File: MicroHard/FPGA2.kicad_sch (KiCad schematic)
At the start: 1 part, among them U4 XC7A100T-FTG256

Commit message: feat: finished config
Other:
- moved on the sheet: U4B
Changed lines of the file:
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@@
 	(symbol
 		(lib_id "FPGA_Xilinx_Artix7:XC7A100T-FTG256")
-		(at 87.63 99.06 0)
+		(at 142.24 91.44 0)
 		(unit 2)
 		(exclude_from_sim no)
@@
 		(fields_autoplaced yes)
 		(property "Reference" "U4"
-			(at 87.63 175.26 0)
+			(at 142.24 167.64 0)
 			(effects
 				(font
@@
 		)
 		(property "Value" "XC7A100T-FTG256"
-			(at 87.63 177.8 0)
+			(at 142.24 170.18 0)
 			(effects
 				(font
@@
 		)
 		(property "Footprint" ""
-			(at 87.63 99.06 0)
+			(at 142.24 91.44 0)
 			(effects
 				(font
@@
 		)
 		(property "Datasheet" ""
-			(at 87.63 99.06 0)
+			(at 142.24 91.44 0)
 			(effects
 				(font
@@
 		)
 		(property "Description" "Artix 7 T 100 XC7A100T-FTG256"
-			(at 87.63 99.06 0)
+			(at 142.24 91.44 0)
 			(effects
 				(font

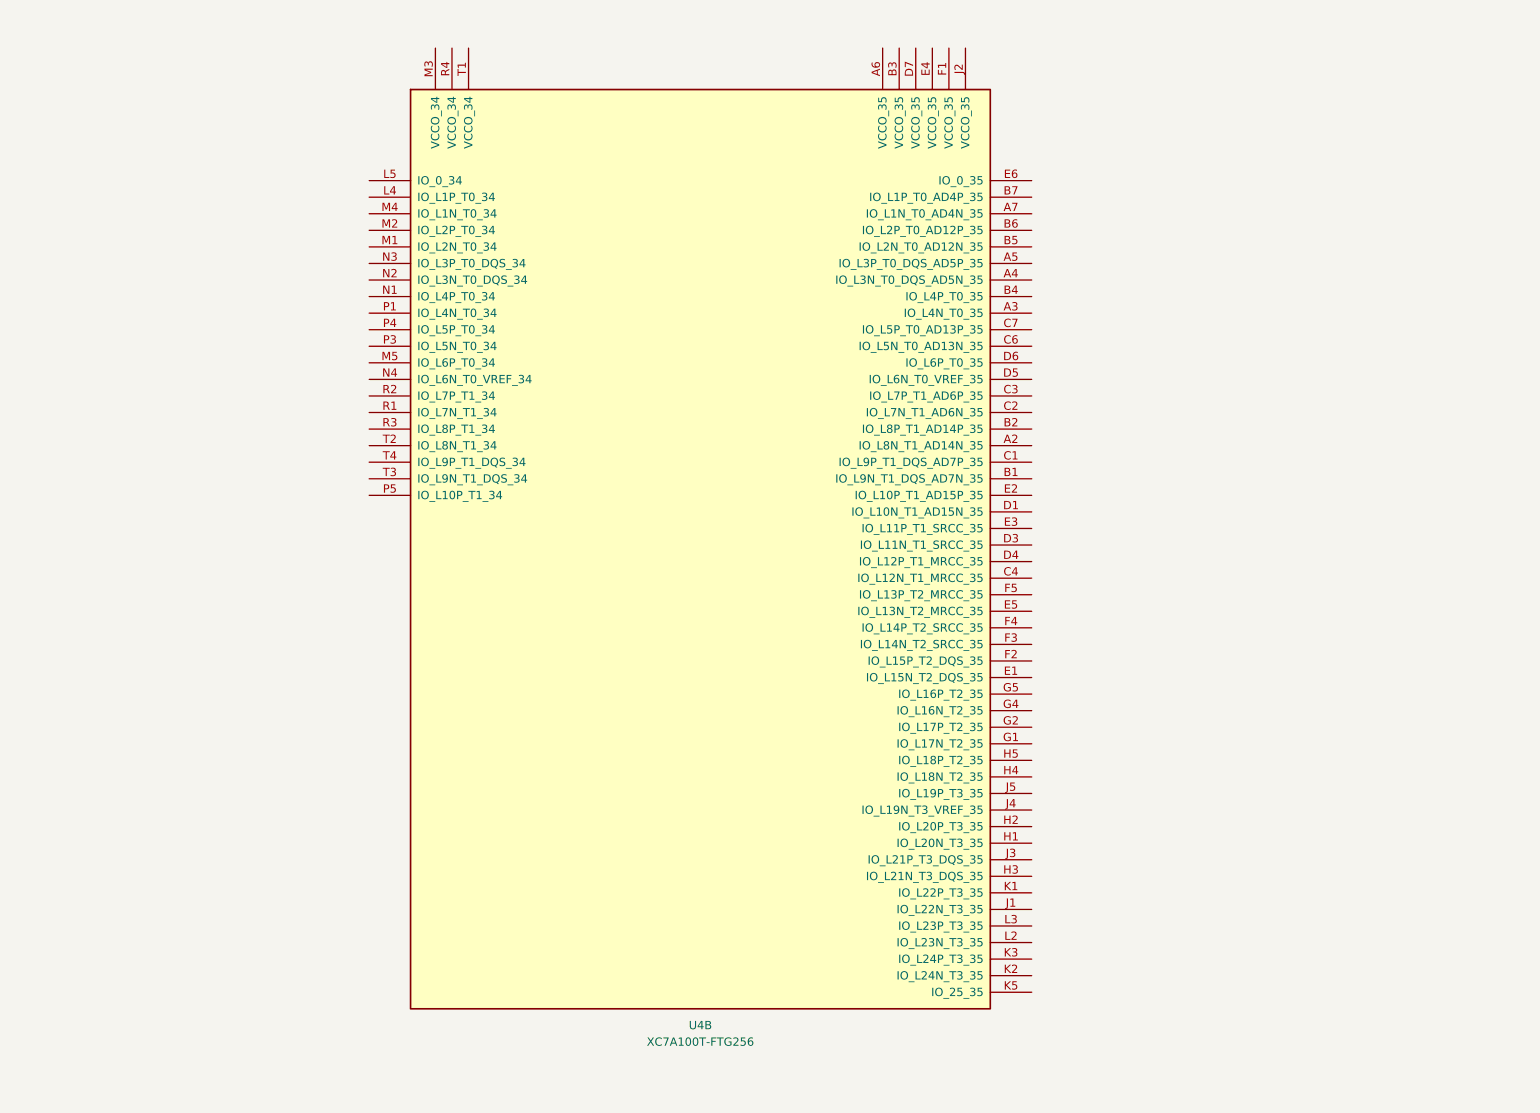
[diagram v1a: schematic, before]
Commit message: feat: added VGA signal out from FPGA
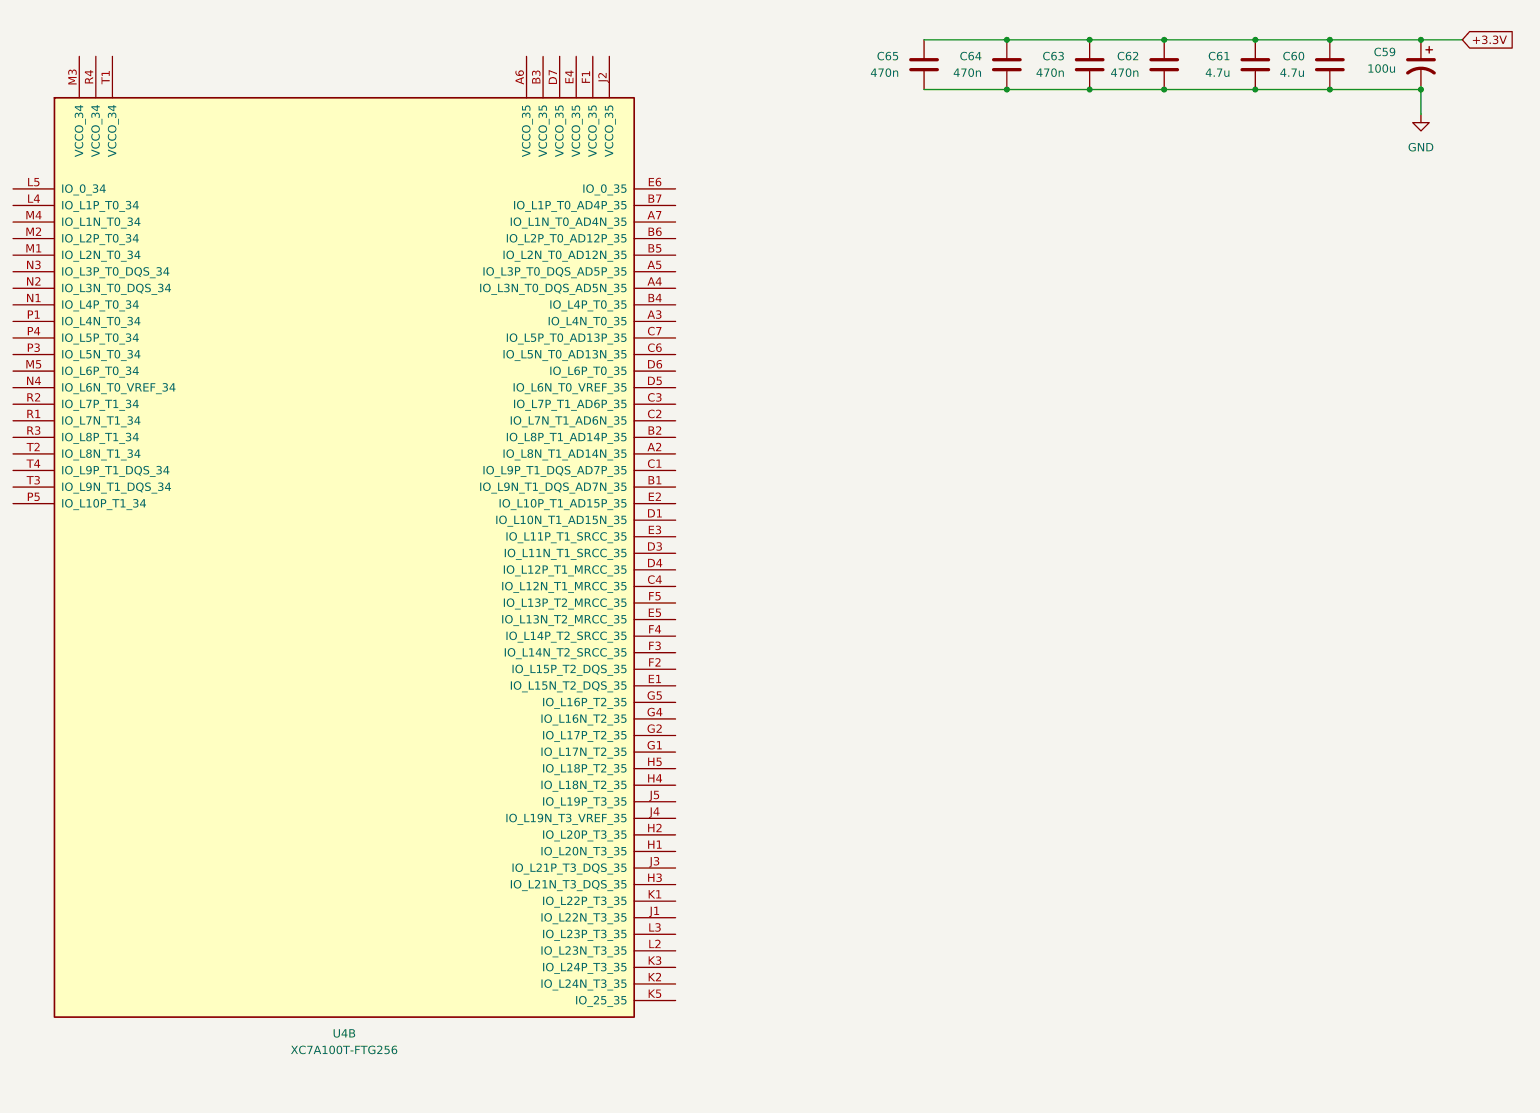
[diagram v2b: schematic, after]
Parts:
- added C59: 100u, symbol Device:C_Polarized_US
- added C60, C61: 4.7u, symbol Device:C
- added C62, C63, C64, C65: 470n, symbol Device:C
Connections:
- new net +3.3V: C59.1, C60.1, C61.1, C62.1, C63.1, C64.1, C65.1
- new net GND: C59.2, C60.2, C61.2, C62.2, C63.2, C64.2, C65.2
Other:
- moved on the sheet: U4B

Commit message: feat: VGA out lines from FPGA drawn
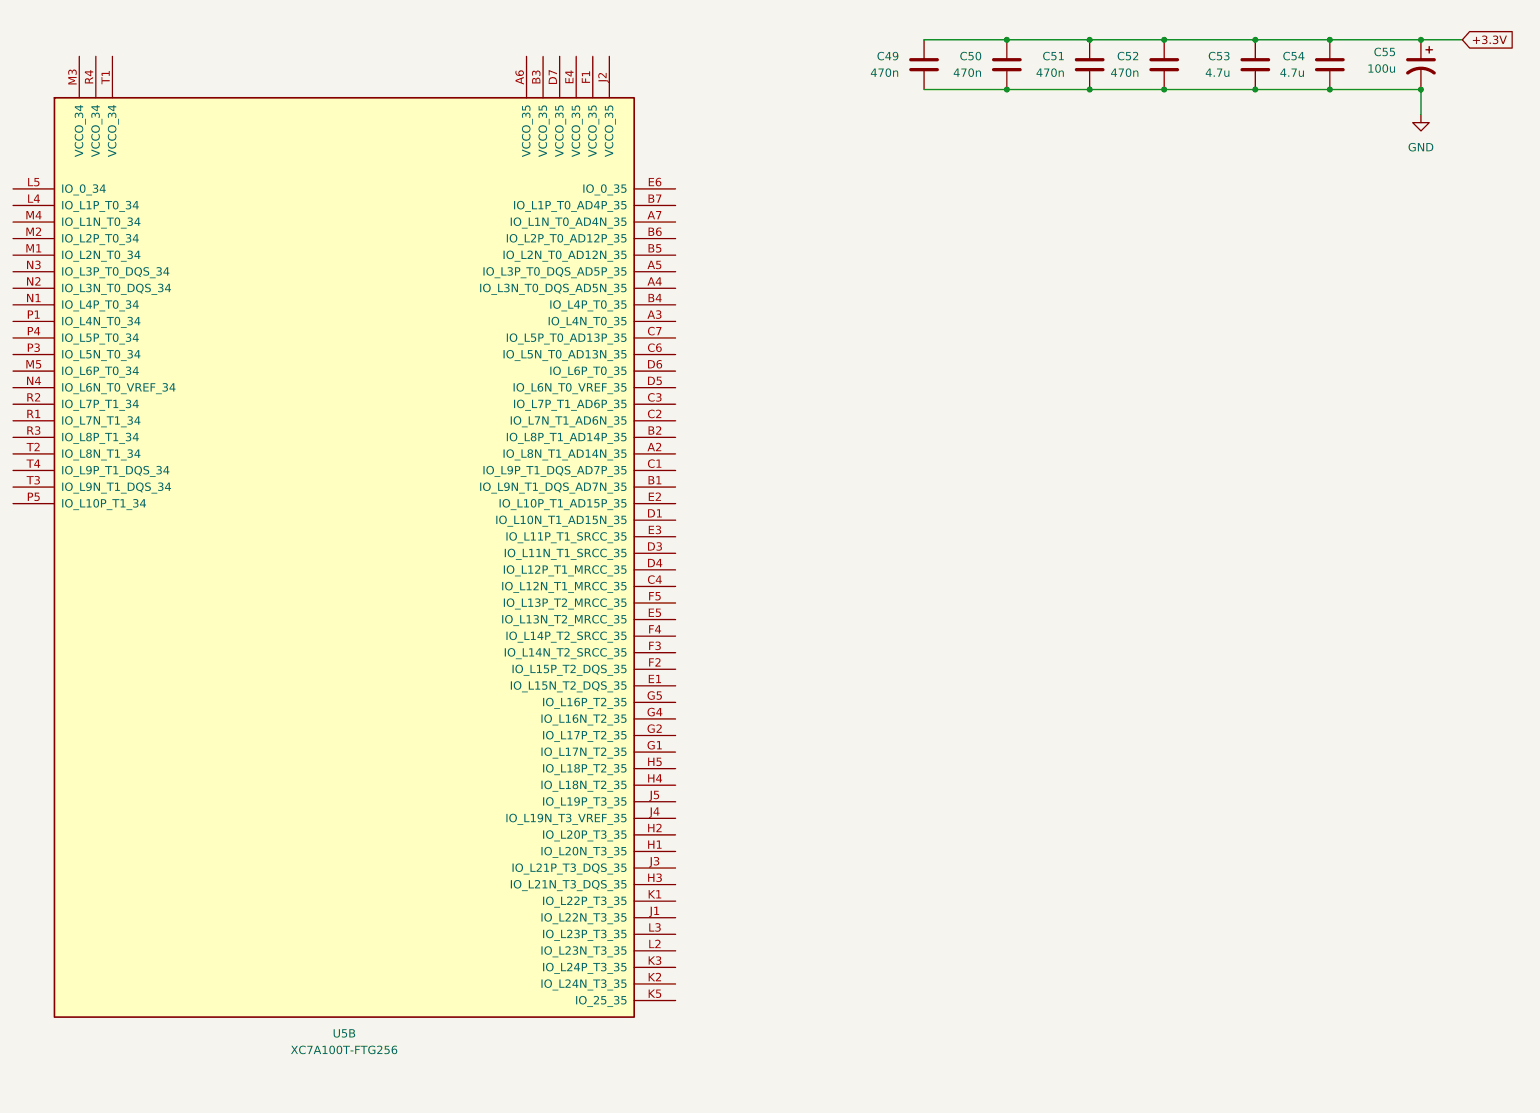
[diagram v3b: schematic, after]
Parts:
- renumbered C65 to C49, C64 to C50, C63 to C51, C62 to C52, C61 to C53, C60 to C54, C59 to C55, U4 to U5
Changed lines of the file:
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@@
 		(dnp no)
 		(fields_autoplaced yes)
-		(property "Reference" "#PWR035"
+		(property "Reference" "#PWR029"
 			(at 252.73 34.29 0)
 			(effects
@@
 			(project "MicroHard"
 				(path "/578bd531-a491-4b15-a479-460d159ffc14/e381883e-e672-4900-88a5-08b94f970a88/3b40193c-1579-4de8-9c25-9c04775413b4"
-					(reference "#PWR035")
+					(reference "#PWR029")
 					(unit 1)
 				)
@@
 		(dnp no)
 		(fields_autoplaced yes)
-		(property "Reference" "C64"
+		(property "Reference" "C50"
 			(at 185.42 19.0499 0)
 			(effects
@@
 			(project "MicroHard"
 				(path "/578bd531-a491-4b15-a479-460d159ffc14/e381883e-e672-4900-88a5-08b94f970a88/3b40193c-1579-4de8-9c25-9c04775413b4"
-					(reference "C64")
+					(reference "C50")
 					(unit 1)
 				)
@@
 		(dnp no)
 		(fields_autoplaced yes)
-		(property "Reference" "U4"
+		(property "Reference" "U5"
 			(at 87.63 168.91 0)
 			(effects
@@
 			(project "MicroHard"
 				(path "/578bd531-a491-4b15-a479-460d159ffc14/e381883e-e672-4900-88a5-08b94f970a88/3b40193c-1579-4de8-9c25-9c04775413b4"
-					(reference "U4")
+					(reference "U5")
 					(unit 2)
 				)
@@
 		(dnp no)
 		(fields_autoplaced yes)
-		(property "Reference" "C60"
+		(property "Reference" "C54"
 			(at 234.95 19.0499 0)
 			(effects
@@
 			(project "MicroHard"
 				(path "/578bd531-a491-4b15-a479-460d159ffc14/e381883e-e672-4900-88a5-08b94f970a88/3b40193c-1579-4de8-9c25-9c04775413b4"
-					(reference "C60")
+					(reference "C54")
 					(unit 1)
 				)
@@
 		(dnp no)
 		(fields_autoplaced yes)
-		(property "Reference" "C59"
+		(property "Reference" "C55"
 			(at 248.92 18.4149 0)
 			(effects
@@
 			(project "MicroHard"
 				(path "/578bd531-a491-4b15-a479-460d159ffc14/e381883e-e672-4900-88a5-08b94f970a88/3b40193c-1579-4de8-9c25-9c04775413b4"
-					(reference "C59")
+					(reference "C55")
 					(unit 1)
 				)
@@
 		(dnp no)
 		(fields_autoplaced yes)
-		(property "Reference" "C62"
+		(property "Reference" "C52"
 			(at 209.55 19.0499 0)
 			(effects
@@
 			(project "MicroHard"
 				(path "/578bd531-a491-4b15-a479-460d159ffc14/e381883e-e672-4900-88a5-08b94f970a88/3b40193c-1579-4de8-9c25-9c04775413b4"
-					(reference "C62")
+					(reference "C52")
 					(unit 1)
 				)
@@
 		(dnp no)
 		(fields_autoplaced yes)
-		(property "Reference" "C65"
+		(property "Reference" "C49"
 			(at 172.72 19.0499 0)
 			(effects
@@
 			(project "MicroHard"
 				(path "/578bd531-a491-4b15-a479-460d159ffc14/e381883e-e672-4900-88a5-08b94f970a88/3b40193c-1579-4de8-9c25-9c04775413b4"
-					(reference "C65")
+					(reference "C49")
 					(unit 1)
 				)
@@
 		(dnp no)
 		(fields_autoplaced yes)
-		(property "Reference" "C61"
+		(property "Reference" "C53"
 			(at 223.52 19.0499 0)
 			(effects
@@
 			(project "MicroHard"
 				(path "/578bd531-a491-4b15-a479-460d159ffc14/e381883e-e672-4900-88a5-08b94f970a88/3b40193c-1579-4de8-9c25-9c04775413b4"
-					(reference "C61")
+					(reference "C53")
 					(unit 1)
 				)
@@
 		(dnp no)
 		(fields_autoplaced yes)
-		(property "Reference" "C63"
+		(property "Reference" "C51"
 			(at 198.12 19.0499 0)
 			(effects
@@
 			(project "MicroHard"
 				(path "/578bd531-a491-4b15-a479-460d159ffc14/e381883e-e672-4900-88a5-08b94f970a88/3b40193c-1579-4de8-9c25-9c04775413b4"
-					(reference "C63")
+					(reference "C51")
 					(unit 1)
 				)

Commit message: feat: finished schematic, TODO: go through checklist
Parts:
- removed C49, C50, C51, C52: 470n, symbol Device:C
- removed C53, C54: 4.7u, symbol Device:C
- removed C55: 100u, symbol Device:C_Polarized_US
- U5: footprint (none) -> MicroHard:BGA256C100P16X16_1700X1700X155
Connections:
- no-connect marks 0 -> 79
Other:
- moved on the sheet: U5B

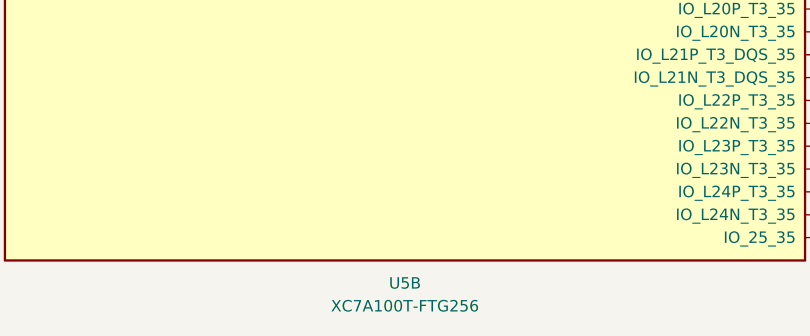
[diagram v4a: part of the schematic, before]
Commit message: Renumber parts
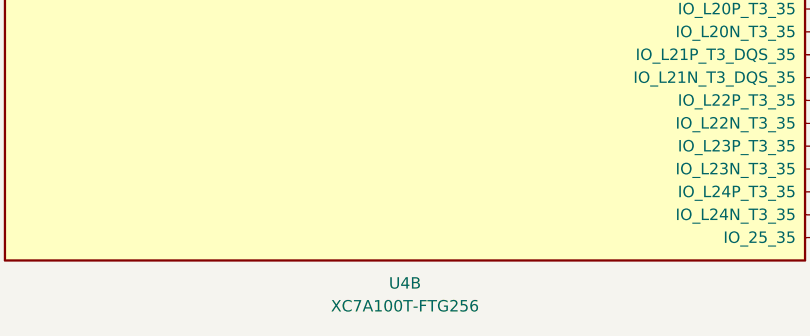
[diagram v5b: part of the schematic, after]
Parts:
- renumbered U5 to U4
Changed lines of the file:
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@@
 		(dnp no)
 		(fields_autoplaced yes)
-		(property "Reference" "U5"
+		(property "Reference" "U4"
 			(at 125.73 167.64 0)
 			(effects
@@
 			(project "MicroHard"
 				(path "/578bd531-a491-4b15-a479-460d159ffc14/e381883e-e672-4900-88a5-08b94f970a88/3b40193c-1579-4de8-9c25-9c04775413b4"
-					(reference "U5")
+					(reference "U4")
 					(unit 2)
 				)

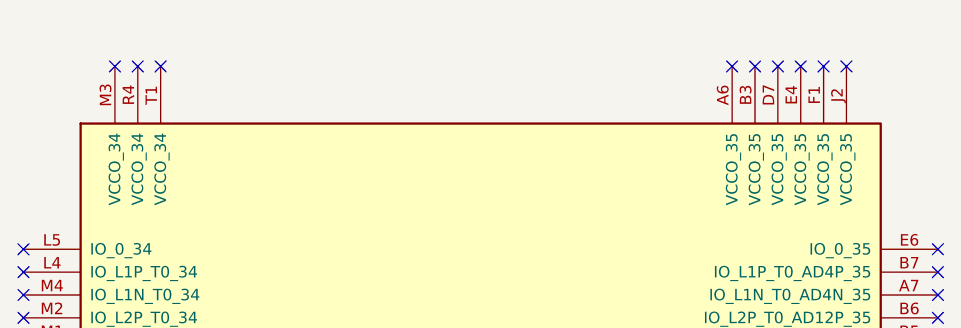
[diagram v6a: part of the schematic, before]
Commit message: power plane
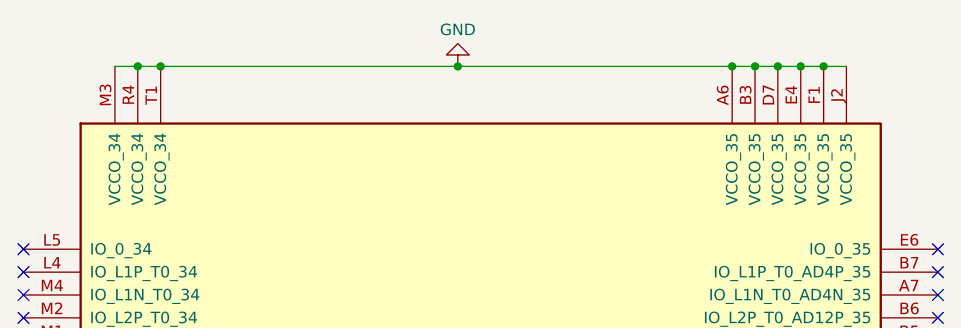
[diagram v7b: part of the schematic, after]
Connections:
- net GND: now reaches U4.A6 (VCCO_35)
- net GND: now also U4.B3 (VCCO_35), U4.D7 (VCCO_35), U4.E4 (VCCO_35), U4.F1 (VCCO_35), U4.J2 (VCCO_35), U4.M3 (VCCO_34), U4.R4 (VCCO_34), U4.T1 (VCCO_34)
- no-connect marks 79 -> 70
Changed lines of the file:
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@@
 	(generator_version "8.0")
 	(paper "A4")
+	(junction
+		(at 153.67 17.78)
+		(diameter 0)
+		(color 0 0 0 0)
+	)
+	(junction
+		(at 161.29 17.78)
+		(diameter 0)
+		(color 0 0 0 0)
+	)
+	(junction
+		(at 163.83 17.78)
+		(diameter 0)
+		(color 0 0 0 0)
+	)
+	(junction
+		(at 90.17 17.78)
+		(diameter 0)
+		(color 0 0 0 0)
+	)
+	(junction
+		(at 123.19 17.78)
+		(diameter 0)
+		(color 0 0 0 0)
+	)
+	(junction
+		(at 87.63 17.78)
+		(diameter 0)
+		(color 0 0 0 0)
+	)
+	(junction
+		(at 158.75 17.78)
+		(diameter 0)
+		(color 0 0 0 0)
+	)
+	(junction
+		(at 156.21 17.78)
+		(diameter 0)
+		(color 0 0 0 0)
+	)
 	(no_connect
 		(at 176.53 68.58)
@@
 	)
 	(no_connect
-		(at 90.17 17.78)
-	)
-	(no_connect
 		(at 176.53 147.32)
 	)
@@
 	)
 	(no_connect
-		(at 156.21 17.78)
-	)
-	(no_connect
-		(at 85.09 17.78)
-	)
-	(no_connect
 		(at 74.93 58.42)
 	)
@@
 	)
 	(no_connect
-		(at 153.67 17.78)
-	)
-	(no_connect
 		(at 74.93 48.26)
 	)
@@
 	)
 	(no_connect
-		(at 163.83 17.78)
-	)
-	(no_connect
 		(at 176.53 129.54)
 	)
@@
 	)
 	(no_connect
-		(at 161.29 17.78)
-	)
-	(no_connect
 		(at 74.93 53.34)
 	)
@@
 	)
 	(no_connect
-		(at 158.75 17.78)
-	)
-	(no_connect
 		(at 176.53 101.6)
 	)
@@
 	)
 	(no_connect
-		(at 166.37 17.78)
-	)
-	(no_connect
 		(at 176.53 63.5)
 	)
@@
 		(at 176.53 160.02)
 	)
-	(no_connect
-		(at 87.63 17.78)
+	(wire
+		(pts
+			(xy 87.63 17.78) (xy 90.17 17.78)
+		)
+		(stroke
+			(width 0)
+			(type default)
+		)
+	)
+	(wire
+		(pts
+			(xy 166.37 17.78) (xy 163.83 17.78)
+		)
+		(stroke
+			(width 0)
+			(type default)
+		)
+	)
+	(wire
+		(pts
+			(xy 153.67 17.78) (xy 123.19 17.78)
+		)
+		(stroke
+			(width 0)
+			(type default)
+		)
+	)
+	(wire
+		(pts
+			(xy 158.75 17.78) (xy 156.21 17.78)
+		)
+		(stroke
+			(width 0)
+			(type default)
+		)
+	)
+	(wire
+		(pts
+			(xy 163.83 17.78) (xy 161.29 17.78)
+		)
+		(stroke
+			(width 0)
+			(type default)
+		)
+	)
+	(wire
+		(pts
+			(xy 156.21 17.78) (xy 153.67 17.78)
+		)
+		(stroke
+			(width 0)
+			(type default)
+		)
+	)
+	(wire
+		(pts
+			(xy 85.09 17.78) (xy 87.63 17.78)
+		)
+		(stroke
+			(width 0)
+			(type default)
+		)
+	)
+	(wire
+		(pts
+			(xy 90.17 17.78) (xy 123.19 17.78)
+		)
+		(stroke
+			(width 0)
+			(type default)
+		)
+	)
+	(wire
+		(pts
+			(xy 161.29 17.78) (xy 158.75 17.78)
+		)
+		(stroke
+			(width 0)
+			(type default)
+		)
 	)
 	(symbol
+		(lib_id "power:GND")
+		(at 123.19 17.78 180)
+		(unit 1)
+		(exclude_from_sim no)
+		(in_bom yes)
+		(on_board yes)
+		(dnp no)
+		(property "Reference" "#PWR072"
+			(at 123.19 11.43 0)
+			(effects
+				(font
+					(size 1.27 1.27)
+				)
+				(hide yes)
+			)
+		)
+		(property "Value" "GND"
+			(at 123.19 13.716 0)
+			(effects
+				(font
+					(size 1.27 1.27)
+				)
+			)
+		)
+		(property "Footprint" ""
+			(at 123.19 17.78 0)
+			(effects
+				(font
+					(size 1.27 1.27)
+				)
+				(hide yes)
+			)
+		)
+		(property "Datasheet" ""
+			(at 123.19 17.78 0)
+			(effects
+				(font
+					(size 1.27 1.27)
+				)
+				(hide yes)
+			)
+		)
+		(property "Description" "Power symbol creates a global label with name \"GND\" , ground"
+			(at 123.19 17.78 0)
+			(effects
+				(font
+					(size 1.27 1.27)
+				)
+				(hide yes)
+			)
+		)
+		(pin "1"
+		)
+		(instances
+			(project ""
+				(path "/578bd531-a491-4b15-a479-460d159ffc14/e381883e-e672-4900-88a5-08b94f970a88/3b40193c-1579-4de8-9c25-9c04775413b4"
+					(reference "#PWR072")
+					(unit 1)
+				)
+			)
+		)
+	)
+	(symbol

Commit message: Fix schematics for delivery
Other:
- company: (none) -> MicroHard
- title: (none) -> FPGA Unit B
